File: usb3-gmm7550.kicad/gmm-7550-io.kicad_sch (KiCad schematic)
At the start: 40 parts, among them J5 10144517-061802LF, J6 Pmod 2x6, SW3 SW_Push, SW4 SW_Push, U10 LSF0204PW, U11 MIC5504-3.3YM5, U9 LSF0204PW

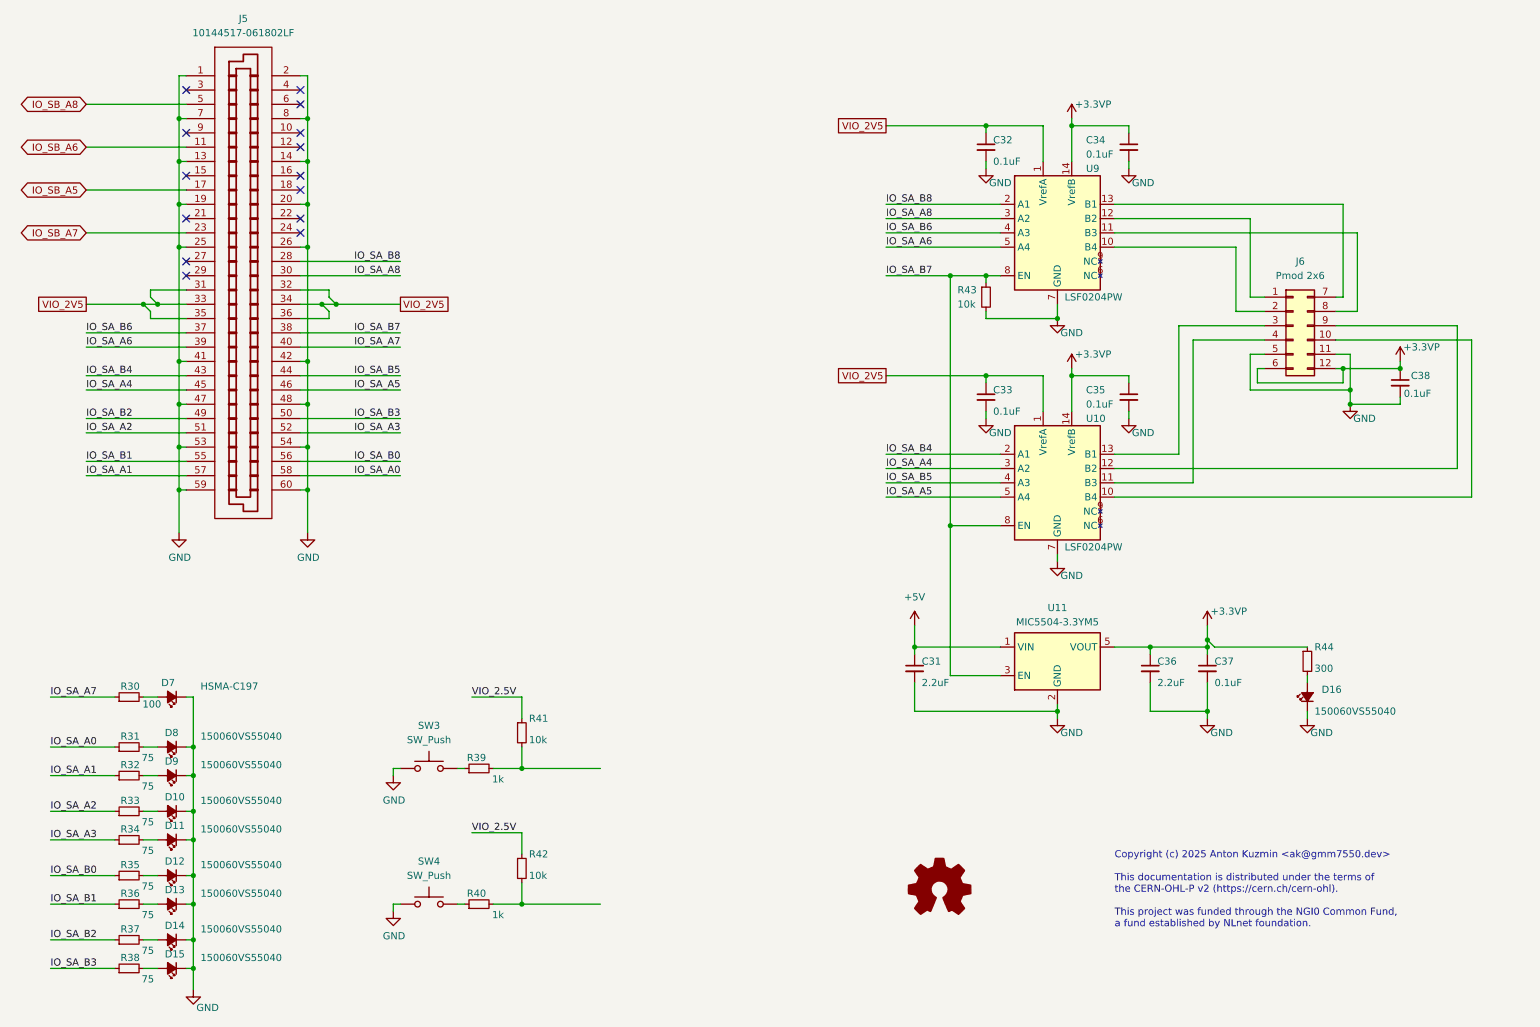
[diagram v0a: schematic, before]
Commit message: USB 3 adapter schematic -- WIP
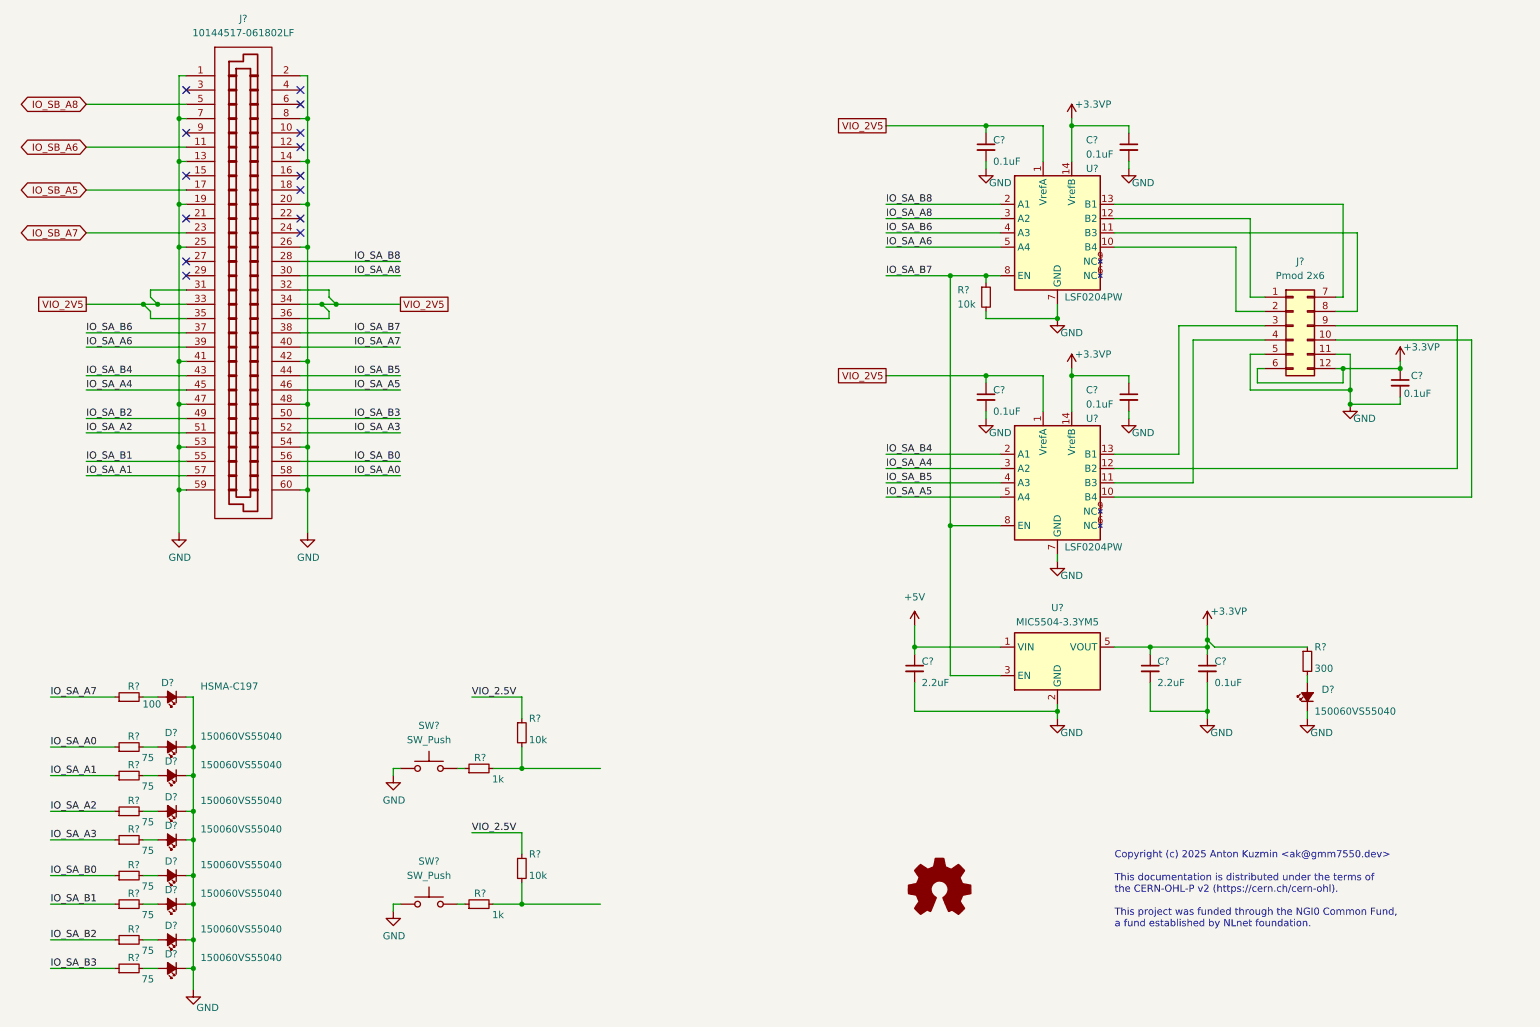
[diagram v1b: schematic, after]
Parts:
- renumbered C38 to C?, C35 to C?, C37 to C?, C33 to C?, C34 to C?, C32 to C?, C36 to C?, C31 to C?, D10 to D?, D9 to D?, D14 to D?, D15 to D?, D13 to D?, D11 to D?, D8 to D?, D12 to D?, D16 to D?, D7 to D?, J6 to J?, J5 to J?, R40 to R?, R35 to R?, R44 to R?, R30 to R?, R33 to R?, R42 to R?, R36 to R?, R41 to R?, R37 to R?, R32 to R?, R39 to R?, R34 to R?, R43 to R?, R31 to R?, R38 to R?, SW3 to SW?, SW4 to SW?, U10 to U?, U9 to U?, U11 to U?

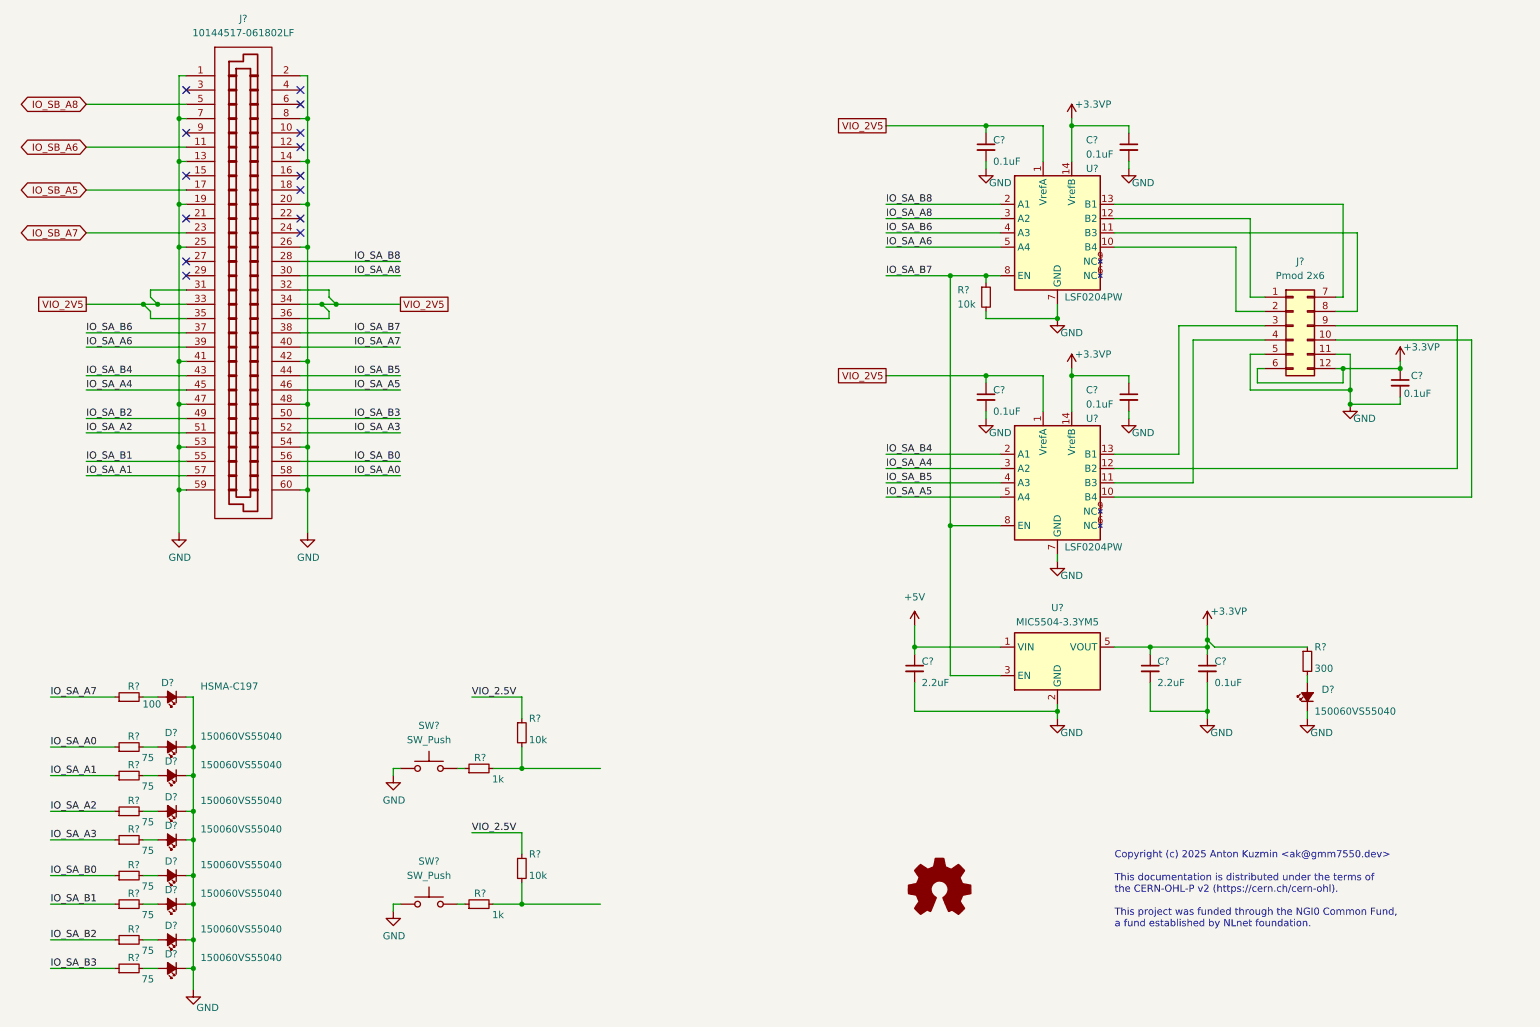
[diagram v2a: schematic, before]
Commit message: USB 3 adapter schematic -- WIP: USB 3 and Power Delivery pages
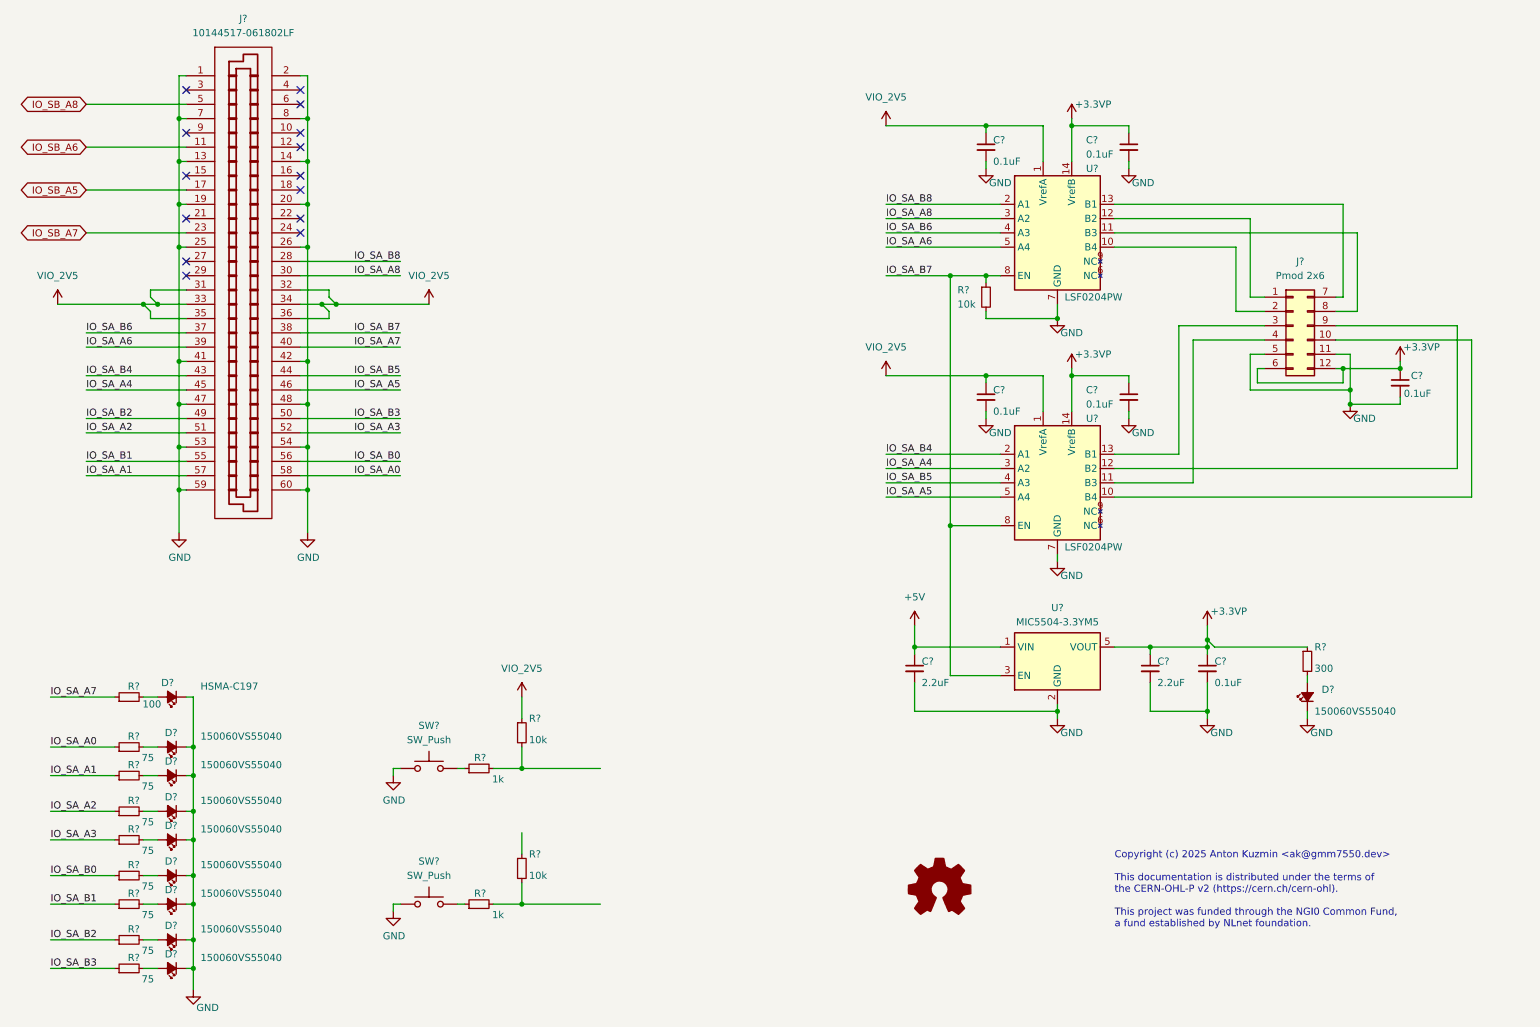
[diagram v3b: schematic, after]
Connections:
- net VIO_2V5: now also R?.1
- net VIO_2.5V: no longer names the net of R?.1
- net VIO_2.5V: no longer R?.1

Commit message: USB 3 adapter schematic -- WIP: USB 1.1 and 2.0 page, connections to the GMM-7550 IOs
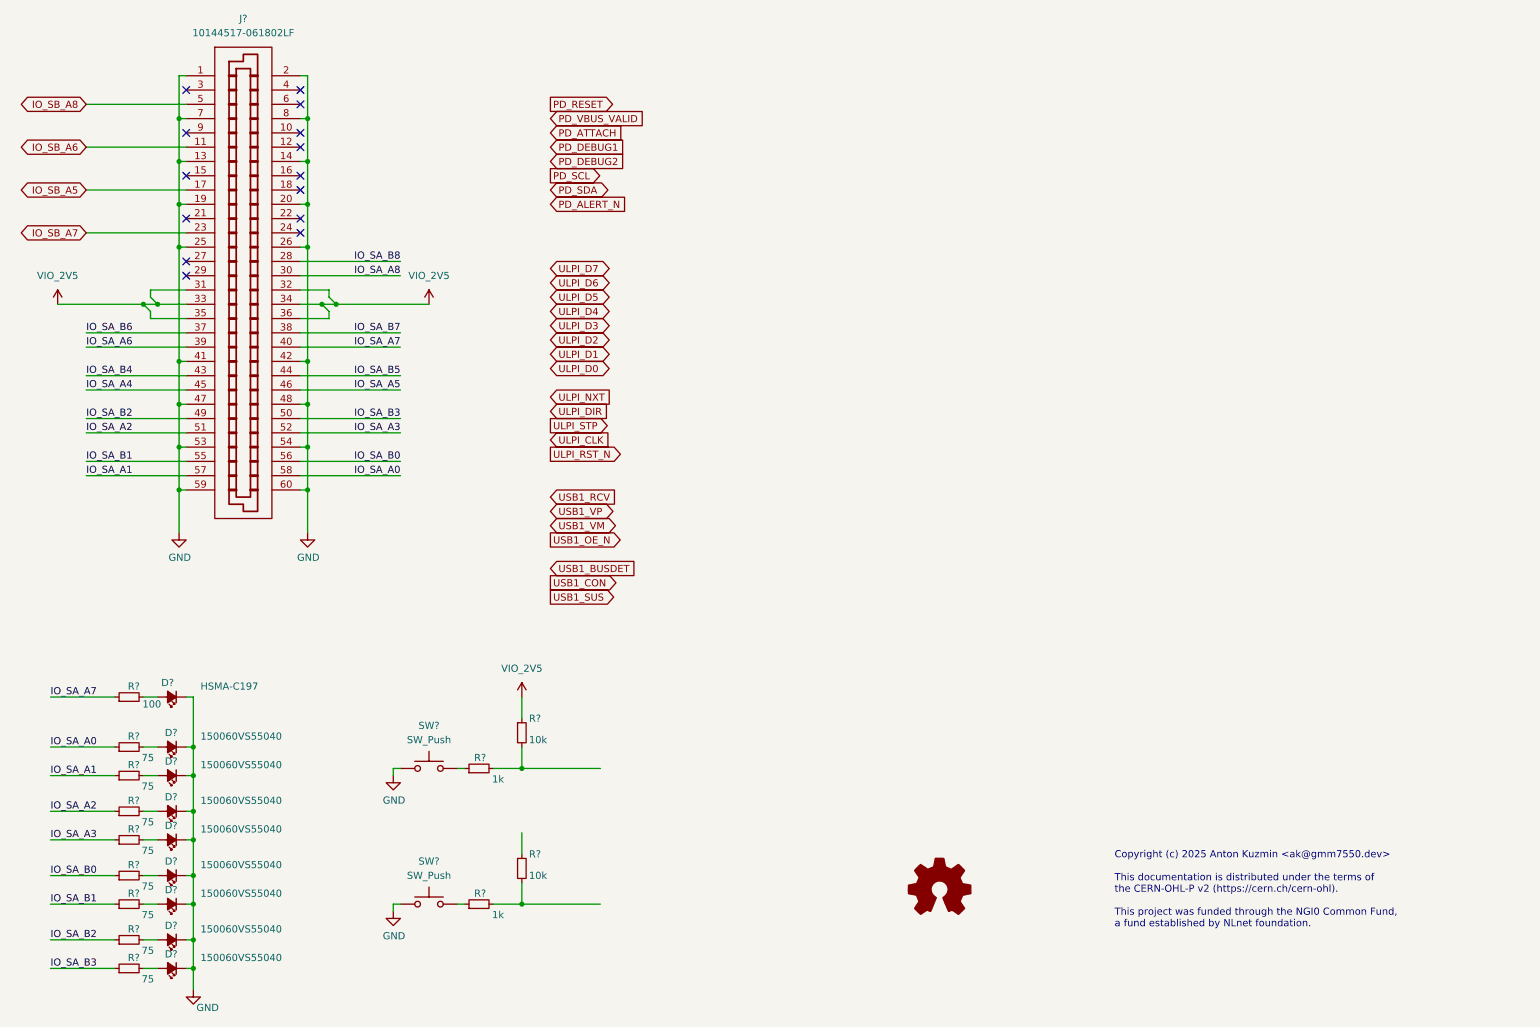
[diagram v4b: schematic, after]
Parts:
- removed C? (x6): 0.1uF, Capacitor_SMD:C_0603_1608Metric, symbol Device:C_Small
- removed C? (x2): 2.2uF, Capacitor_SMD:C_0603_1608Metric, symbol Device:C_Small
- removed D?: 150060VS55040, LED_SMD:LED_0603_1608Metric, symbol Device:LED_Small_Filled
- removed J?: Pmod 2x6, Pmod:PmodSocket_2x06_P2.54mm_Horizontal, symbol Connector_Generic:Conn_02x06_Top_Bottom
- removed R?: 300, Resistor_SMD:R_0603_1608Metric, symbol Device:R_Small
- removed R?: 10k, Resistor_SMD:R_0603_1608Metric, symbol Device:R_Small
- removed U? (x2): LSF0204PW, Package_SO:TSSOP-14_4.4x5mm_P0.65mm, symbol hat-gmm7550:LSF0204PW
- removed U?: MIC5504-3.3YM5, Package_TO_SOT_SMD:SOT-23-5, symbol Regulator_Linear:MIC5504-3.3YM5
